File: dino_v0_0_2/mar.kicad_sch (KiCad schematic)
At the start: 10 parts, among them U54 74LS245, U55 74LS373, U58 74LS373, U59 74LS245, U60 74LS02

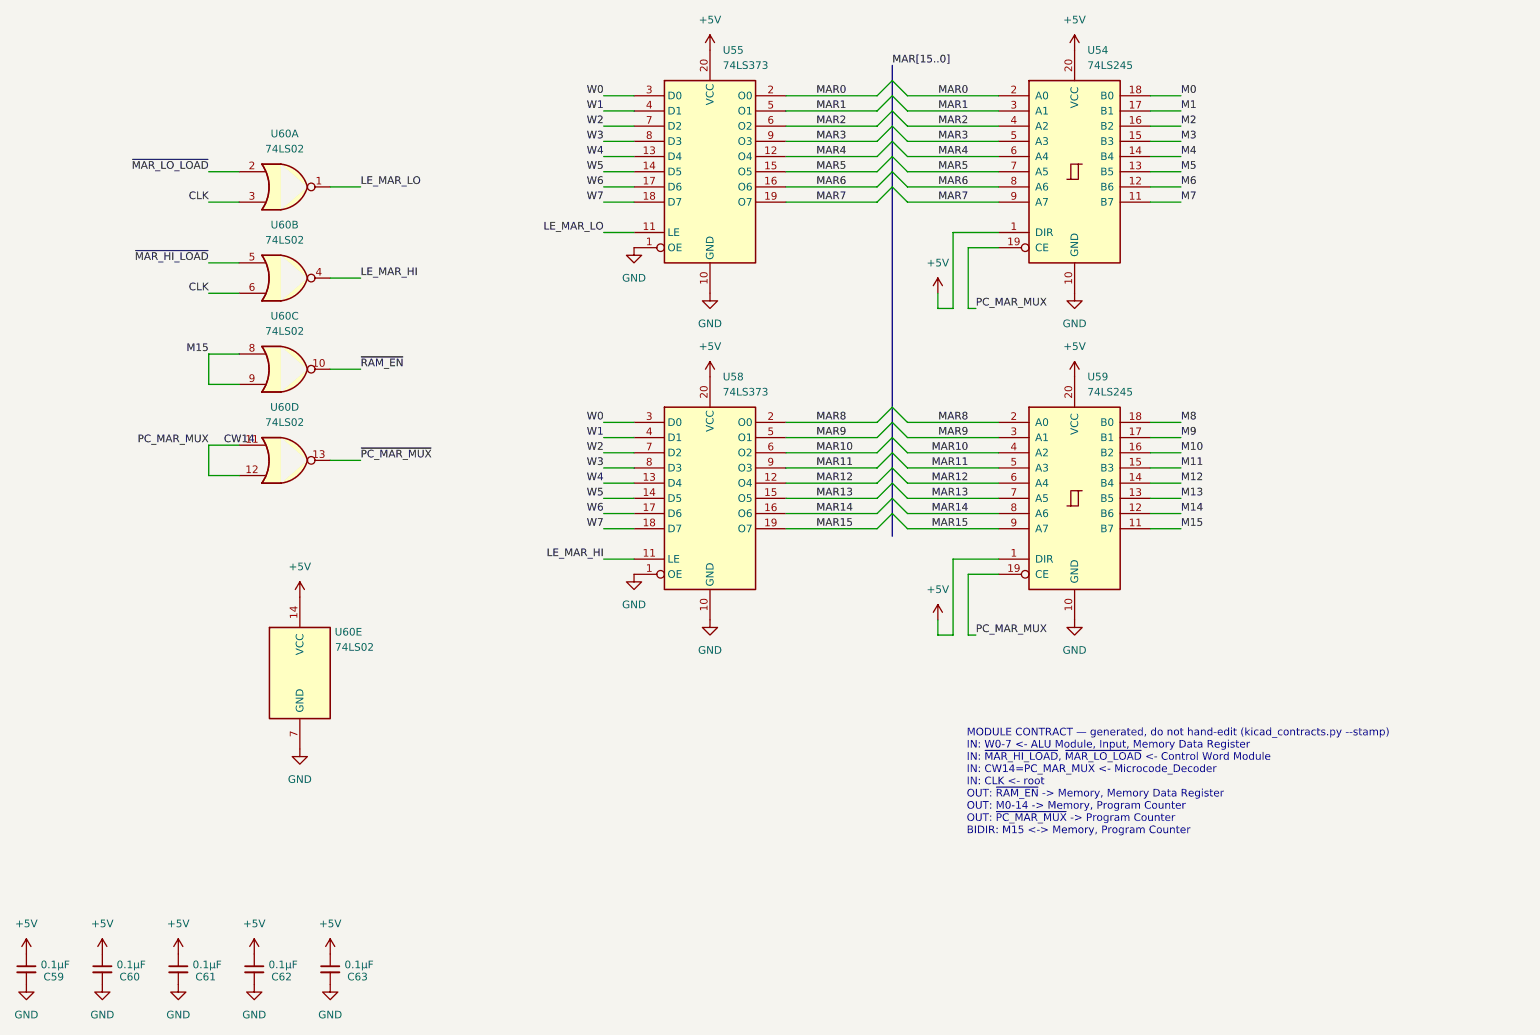
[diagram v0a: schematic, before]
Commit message: feat(kicad): footprints, power sheet, global labels, PCB draft
Every symbol gets a stock THT footprint (plain DIP, no sockets, so the
3D render shows ICs). New Power sheet: 24-pin ATX header for a picoPSU,
rails +5V/+3.3V/+12V/-12V/GND only; no -5V exists on any ATX unit since
2003, none drawn. PS_ON# on a 2-pin header.

Cross-sheet labels become global labels. KiCad joined nothing between
sheets before: 122 base names were split per sheet, ERC saw 90 undriven
inputs whose driver sat one sheet away, and the PCB ratsnest stopped at
every sheet boundary. Proof: KiCad's netlist after equals a name-join of
its netlist before plus the 15 CW alias pairs, pin for pin.

kicad_contracts took a node's sheet from the net name's /Sheet/ prefix;
global nets have none, so it emitted an empty contracts doc. Sheet now
comes from the component's own path; the doc regenerates with zero diff.

ERC 477 -> 2. Real fixes: ROM I/O pins input -> tri_state, '382 GND pin
power_out -> power_in, four orphan symbols rehomed to project lib `dino`,
one stub wire. 133 by-design warnings excluded by uuid ('245 readback on
counter Q, alias stubs, probe-point labels); the two left are bus
signals the peripheral bus sheet will consume.

PCB draft: 198 footprints placed per sheet, all pads netted, no tracks.

Co-Authored-By: Claude Fable 5.1 <noreply@anthropic.com>
Claude-Session: https://claude.ai/code/session_018irreFHb1xEykW5kCD26ow
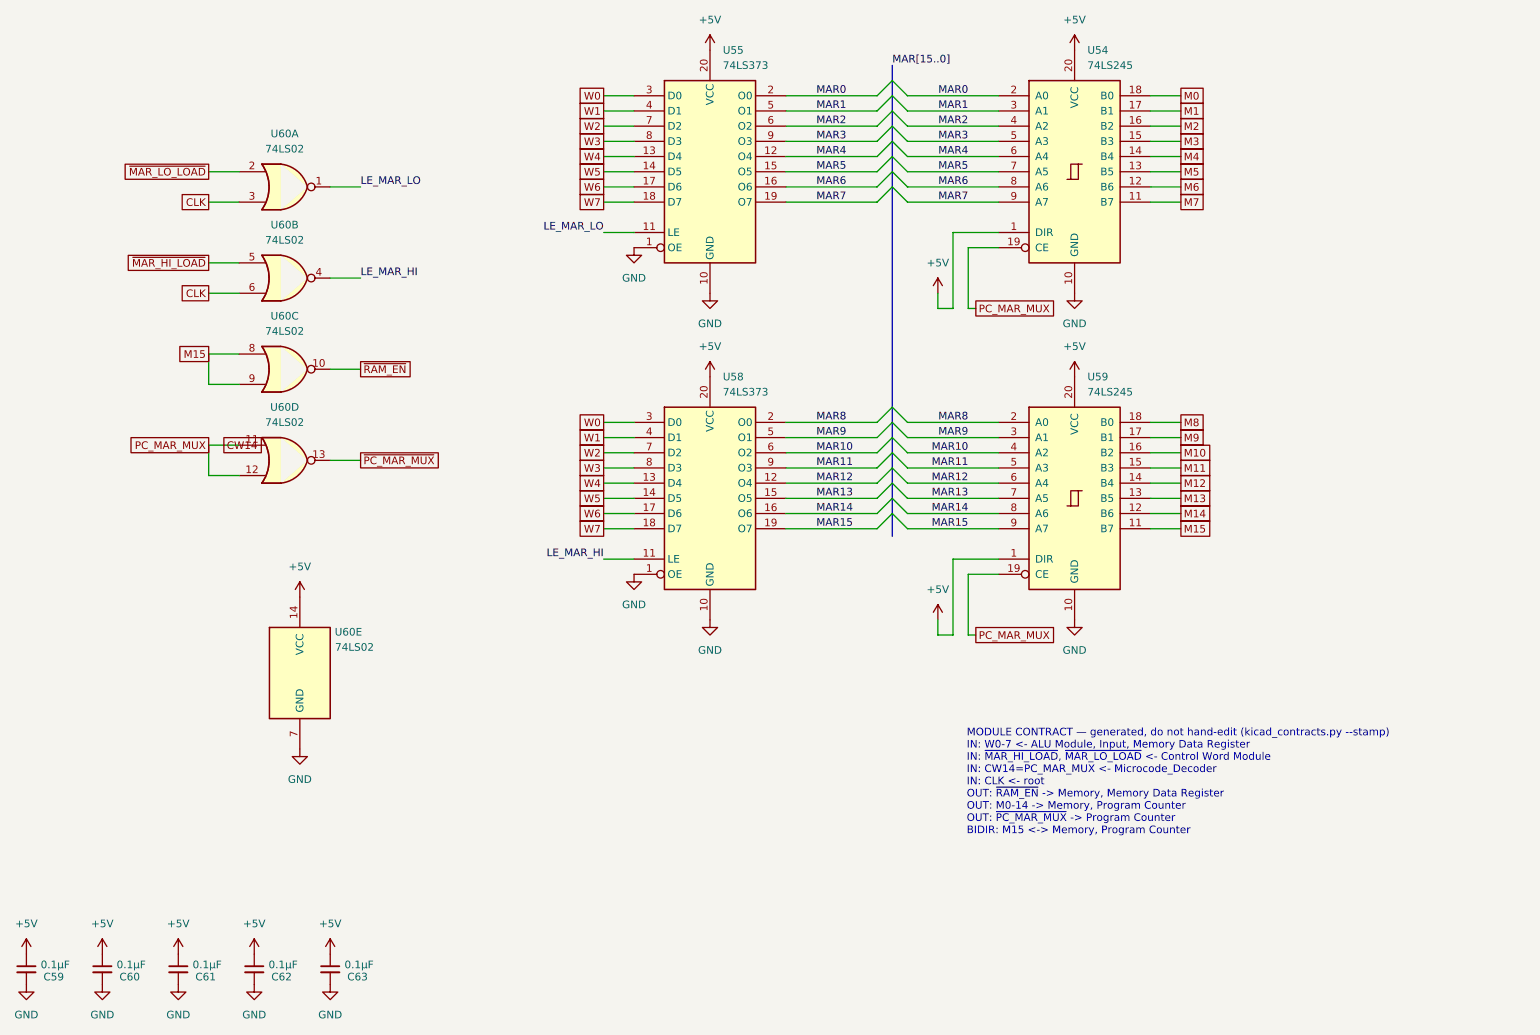
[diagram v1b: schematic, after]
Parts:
- C59, C60, C61, C62, C63: footprint (none) -> Capacitor_THT:C_Disc_D5.0mm_W2.5mm_P2.50mm
- U54, U55, U58, U59: footprint (none) -> Package_DIP:DIP-20_W7.62mm
- U60: footprint (none) -> Package_DIP:DIP-14_W7.62mm

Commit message: feat(int): draw the interrupt block; sheet cleanup pass
New sheet dino_v0_0_2/interrupt.kicad_sch (page 15): U80-U87, R28 4.7k
pull-up on ~{IRQ}, R29 100R on the block's CLK branch, C83-C90. Every
pin per PHASE_INT SECTION 3, checked against the plan with kicad_netlist
and kicad-cli (146 pins, 0 mismatches).

Old sheets (SECTION 3.2): U28.4 lifted off GND to INJECT; U61.3 to
END_OR_ACCEPT; U36.1 to PC_UP_GATED; U49 D0-3 cut from U48 Za-Zd and
routed through U87 as FLAG_NEXT0-3 / FLAG_D0-3; FLAG_C/Z/V/N and the
five decoder outputs made global. dino_serial: U104 74LS05, INTR ->
~{IRQ}, C4.

Placement pass on every sheet: bus entries and global labels no longer
share wires; M, CW, T, IRB and SA buses kept as labelled keys. Nets
diffed against HEAD per sheet: only the intended changes and a rotated
C29. Project ERC: 0 errors. MODULE CONTRACT stamps regenerated.

Co-Authored-By: Claude Fable 5.1 <noreply@anthropic.com>
Claude-Session: https://claude.ai/code/session_01JGxSS4MVUcaZdKZGtKroSg
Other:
- note added: "MODULE CONTRACT — generated, do not hand-edit (kicad_contracts.py --stamp) IN: W0-7 <- ALU Module, Memory Data Register IN: ~{MAR_HI_LOAD}, ~{MAR_LO_LOAD} <- Control Word Module IN: CW14=PC_MAR_MUX <- Microcode_Decoder IN: CLK <- root OUT: ~{RAM_EN} -> Memory, Memory Data Register OUT: M0-14 -> Memory, Peripheral Bus, Program Counter OUT: ~{PC_MAR_MUX} -> Program Counter BIDIR: M15 <-> Memory, Pe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"
- note removed: "MODULE CONTRACT — generated, do not hand-edit (kicad_contracts.py --stamp) IN: W0-7 <- ALU Module, Input, Memory Data Register IN: ~{MAR_HI_LOAD}, ~{MAR_LO_LOAD} <- Control Word Module IN: CW14=PC_MAR_MUX <- Microcode_Decoder IN: CLK <- root OUT: ~{RAM_EN} -> Memory, Memory Data Register OUT: M0-14 -> Memory, Program Counter OUT: ~{PC_MAR_MUX} -> Program Counter BIDIR: M15 <-> Memory, Program Cou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"
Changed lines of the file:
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@@
 		(comment 4 "A Turing-Complete 8-bit \"Computer\"")
 	)
-	(text "MODULE CONTRACT — generated, do not hand-edit (kicad_contracts.py --stamp)\nIN: W0-7 <- ALU Module, Input, Memory Data Register\nIN: ~{MAR_HI_LOAD}, ~{MAR_LO_LOAD} <- Control Word Module\nIN: CW14=PC_MAR_MUX <- Microcode_Decoder\nIN: CLK <- root\nOUT: ~{RAM_EN} -> Memory, Memory Data Register\nOUT: M0-14 -> Memory, Program Counter\nOUT: ~{PC_MAR_MUX} -> Program Counter\nBIDIR: M15 <-> Memory, Program Counter"
+	(text "MODULE CONTRACT — generated, do not hand-edit (kicad_contracts.py --stamp)\nIN: W0-7 <- ALU Module, Memory Data Register\nIN: ~{MAR_HI_LOAD}, ~{MAR_LO_LOAD} <- Control Word Module\nIN: CW14=PC_MAR_MUX <- Microcode_Decoder\nIN: CLK <- root\nOUT: ~{RAM_EN} -> Memory, Memory Data Register\nOUT: M0-14 -> Memory, Peripheral Bus, Program Counter\nOUT: ~{PC_MAR_MUX} -> Program Counter\nBIDIR: M15 <-> Memory, Peripheral Bus, Program Counter"
 		(exclude_from_sim no)
 		(at 177.546 164.338 0)
@@
 	(global_label "CW14"
 		(shape passive)
-		(at 53.34 99.06 0)
+		(at 50.8 104.14 180)
 		(fields_autoplaced yes)
 		(effects
@@
 				(size 1.27 1.27)
 			)
-			(justify left)
+			(justify right)
 		)
 		(property "Intersheetrefs" "${INTERSHEET_REFS}"
-			(at 53.34 99.06 0)
+			(at 50.8 104.14 0)
 			(hide yes)
 			(show_name no)
@@
 					(size 1.27 1.27)
 				)
-				(justify left)
-			)
-		)
+				(justify right)
+			)
+		)
